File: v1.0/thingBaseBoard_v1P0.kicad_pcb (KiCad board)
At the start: 2 copper layers, 222 x 75 mm, 66 parts, among them P1 3_Pin_Screw_Connector, P2 16_PIN_IDC_HEADER, P3 8_Pin Screw Connector, Q1 2N3904-MMBT, Q2 2N3904-MMBT, Q3 2N3904-MMBT, Q4 2N3904-MMBT, Q5 2N3904-MMBT, Q6 2N3904-MMBT, Q7 2N7002, U1 HenLv-AC220S3_3DCS-3W, U2 DF08S1_BRIDGE_REC-IC, U3 XBEE_MODULE, U4 TRIAC_BOARD, U5 4N35_OPTO, U6 TRIAC_BOARD

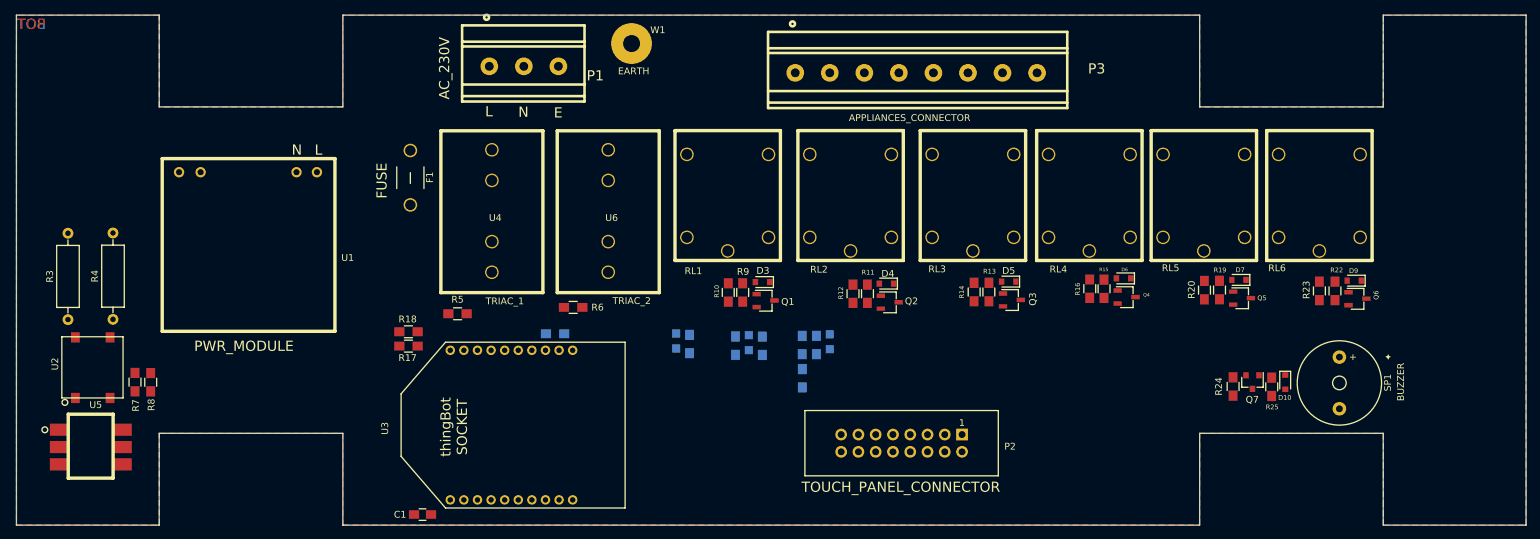
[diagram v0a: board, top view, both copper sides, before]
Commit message: Routing done
routing Completed,
Power Module footprint Changed,
2mm size of the PCB reduced.
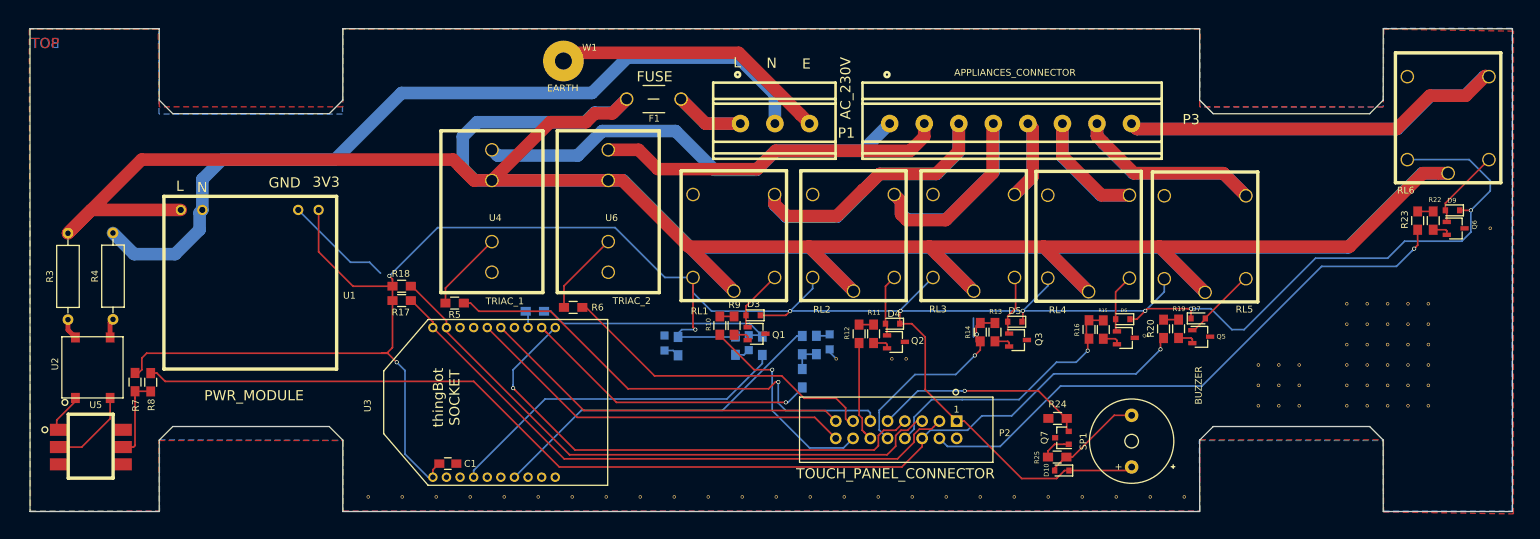
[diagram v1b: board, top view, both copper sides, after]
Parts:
- added REF**: VIA_0.5mm, via:VIA_0.5mm, F.Cu at (198.7, 126.3)
- added REF**: VIA_0.5mm, via:VIA_0.5mm, F.Cu at (153.7, 126.3)
- added REF**: VIA_0.5mm, via:VIA_0.5mm, F.Cu at (148.7, 126.3)
- added REF**: VIA_0.5mm, via:VIA_0.5mm, F.Cu at (143.7, 126.3)
- added REF**: VIA_0.5mm, via:VIA_0.5mm, F.Cu at (138.7, 126.3)
- added REF**: VIA_0.5mm, via:VIA_0.5mm, F.Cu at (133.7, 126.3)
- added REF**: VIA_0.5mm, via:VIA_0.5mm, F.Cu at (128.7, 126.3)
- added REF**: VIA_0.5mm, via:VIA_0.5mm, F.Cu at (123.7, 126.3)
- added REF**: VIA_0.5mm, via:VIA_0.5mm, F.Cu at (118.7, 126.3)
- added REF**: VIA_0.5mm, via:VIA_0.5mm, F.Cu at (113.7, 126.3)
- added REF**: VIA_0.5mm, via:VIA_0.5mm, F.Cu at (108.7, 126.3)
- added REF**: VIA_0.5mm, via:VIA_0.5mm, F.Cu at (193.7, 126.3)
- added REF**: VIA_0.5mm, via:VIA_0.5mm, F.Cu at (103.7, 126.3)
- added REF**: VIA_0.5mm, via:VIA_0.5mm, F.Cu at (98.7, 126.3)
- added REF**: VIA_0.5mm, via:VIA_0.5mm, F.Cu at (93.7, 126.3)
- added REF**: VIA_0.5mm, via:VIA_0.5mm, F.Cu at (88.7, 126.3)
- added REF**: VIA_0.5mm, via:VIA_0.5mm, F.Cu at (83.7, 126.3)
- added REF**: VIA_0.5mm, via:VIA_0.5mm, F.Cu at (78.7, 126.3)
- added REF**: VIA_0.5mm, via:VIA_0.5mm, F.Cu at (215.6, 106.9)
- added REF**: VIA_0.5mm, via:VIA_0.5mm, F.Cu at (209.6, 106.9)
- added REF**: VIA_0.5mm, via:VIA_0.5mm, F.Cu at (212.6, 106.9)
- added REF**: VIA_0.5mm, via:VIA_0.5mm, F.Cu at (215.6, 112.9)
- added REF**: VIA_0.5mm, via:VIA_0.5mm, F.Cu at (188.7, 126.3)
- added REF**: VIA_0.5mm, via:VIA_0.5mm, F.Cu at (212.6, 112.9)
- added REF**: VIA_0.5mm, via:VIA_0.5mm, F.Cu at (209.6, 112.9)
- added REF**: VIA_0.5mm, via:VIA_0.5mm, F.Cu at (215.6, 109.9)
- added REF**: VIA_0.5mm, via:VIA_0.5mm, F.Cu at (212.6, 109.9)
- added REF**: VIA_0.5mm, via:VIA_0.5mm, F.Cu at (209.6, 109.9)
- added REF**: VIA_0.5mm, via:VIA_0.5mm, F.Cu at (234.6, 112.9)
- added REF**: VIA_0.5mm, via:VIA_0.5mm, F.Cu at (231.6, 112.9)
- added REF**: VIA_0.5mm, via:VIA_0.5mm, F.Cu at (228.6, 112.9)
- added REF**: VIA_0.5mm, via:VIA_0.5mm, F.Cu at (225.6, 112.9)
- added REF**: VIA_0.5mm, via:VIA_0.5mm, F.Cu at (222.6, 112.9)
- added REF**: VIA_0.5mm, via:VIA_0.5mm, F.Cu at (183.7, 126.3)
- added REF**: VIA_0.5mm, via:VIA_0.5mm, F.Cu at (234.6, 109.9)
- added REF**: VIA_0.5mm, via:VIA_0.5mm, F.Cu at (231.6, 109.9)
- added REF**: VIA_0.5mm, via:VIA_0.5mm, F.Cu at (228.6, 109.9)
- added REF**: VIA_0.5mm, via:VIA_0.5mm, F.Cu at (225.6, 109.9)
- added REF**: VIA_0.5mm, via:VIA_0.5mm, F.Cu at (222.6, 109.9)
- added REF**: VIA_0.5mm, via:VIA_0.5mm, F.Cu at (234.6, 106.9)
- added REF**: VIA_0.5mm, via:VIA_0.5mm, F.Cu at (231.6, 106.9)
- added REF**: VIA_0.5mm, via:VIA_0.5mm, F.Cu at (228.6, 106.9)
- added REF**: VIA_0.5mm, via:VIA_0.5mm, F.Cu at (225.6, 106.9)
- added REF**: VIA_0.5mm, via:VIA_0.5mm, F.Cu at (222.6, 106.9)
- added REF**: VIA_0.5mm, via:VIA_0.5mm, F.Cu at (178.7, 126.3)
- added REF**: VIA_0.5mm, via:VIA_0.5mm, F.Cu at (234.6, 103.9)
- added REF**: VIA_0.5mm, via:VIA_0.5mm, F.Cu at (231.6, 103.9)
- added REF**: VIA_0.5mm, via:VIA_0.5mm, F.Cu at (228.6, 103.9)
- added REF**: VIA_0.5mm, via:VIA_0.5mm, F.Cu at (225.6, 103.9)
- added REF**: VIA_0.5mm, via:VIA_0.5mm, F.Cu at (222.6, 103.9)
- added REF**: VIA_0.5mm, via:VIA_0.5mm, F.Cu at (234.6, 100.9)
- added REF**: VIA_0.5mm, via:VIA_0.5mm, F.Cu at (231.6, 100.9)
- added REF**: VIA_0.5mm, via:VIA_0.5mm, F.Cu at (228.6, 100.9)
- added REF**: VIA_0.5mm, via:VIA_0.5mm, F.Cu at (225.6, 100.9)
- added REF**: VIA_0.5mm, via:VIA_0.5mm, F.Cu at (222.6, 100.9)
- added REF**: VIA_0.5mm, via:VIA_0.5mm, F.Cu at (173.7, 126.3)
- added REF**: VIA_0.5mm, via:VIA_0.5mm, F.Cu at (234.6, 97.9)
- added REF**: VIA_0.5mm, via:VIA_0.5mm, F.Cu at (231.6, 97.9)
- added REF**: VIA_0.5mm, via:VIA_0.5mm, F.Cu at (228.6, 97.9)
- added REF**: VIA_0.5mm, via:VIA_0.5mm, F.Cu at (225.6, 97.9)
- added REF**: VIA_0.5mm, via:VIA_0.5mm, F.Cu at (222.6, 97.9)
- added REF**: VIA_0.5mm, via:VIA_0.5mm, F.Cu at (155.7, 106.0)
- added REF**: VIA_0.5mm, via:VIA_0.5mm, F.Cu at (157.8, 106.0)
- added REF**: VIA_0.5mm, via:VIA_0.5mm, F.Cu at (147.5, 106.0)
- added REF**: VIA_0.5mm, via:VIA_0.5mm, F.Cu at (243.7, 86.8)
- added REF**: Fab Details table, Fab Details table:Fab Details table, F.Cu at (38.0, 145.6)
- added REF**: VIA_0.5mm, via:VIA_0.5mm, F.Cu at (168.7, 126.3)
- added REF**: VIA_0.5mm, via:VIA_0.5mm, F.Cu at (163.7, 126.3)
- added REF**: VIA_0.5mm, via:VIA_0.5mm, F.Cu at (158.7, 126.3)
- P1: value 3_Pin_Screw_Connector -> AC_230V
- P2: value 16_PIN_IDC_HEADER -> TOUCH_PANEL_CONNECTOR
- P3: value 8_Pin Screw Connector -> APPLIANCES_CONNECTOR
- moved F1 40.5 mm to (124.7, 67.8), turned to 180 degrees
- moved P1 37.9 mm to (133.4, 71.4)
- moved D10 35.3 mm to (180.7, 122.4), turned to 180 degrees
- moved R25 33.2 mm to (180.0, 120.4), turned to 0 degrees
- moved SP1 31.7 mm to (191.0, 118.1), turned to 90 degrees
- moved Q7 29.2 mm to (180.7, 117.6), turned to 180 degrees
- moved R24 26.2 mm to (180.1, 114.8), turned to 0 degrees
- moved RL6 22.1 mm to (245.6, 80.6)
- moved D9 17.8 mm to (238.2, 84.2)
- moved Q6 17.8 mm to (238.6, 86.8)
- moved R23 17.8 mm to (233.0, 85.7)
- moved R22 17.8 mm to (235.3, 85.7)
- moved P3 15.8 mm to (155.4, 71.4)
- moved W1 10.3 mm to (107.4, 62.2)
- moved C1 8.37 mm to (90.4, 121.4), turned to 0 degrees
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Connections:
- U1 pad 1: Net-(F1-Pad1) -> L
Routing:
- net L: track 0.00 -> 540.5 mm
- net +3V3: track 0.00 -> 403.3 mm, vias 0 -> 9
- net RELAY_5: track 0.00 -> 163.9 mm, vias 0 -> 1
- net N: track 0.00 -> 121.3 mm
- net Net-(P3-Pad8): track 0.00 -> 112.2 mm
- net I2C_SDA: track 0.00 -> 90.8 mm
- net I2C_SCL: track 0.00 -> 89.5 mm
- net RELAY_6: track 0.00 -> 85.3 mm, vias 0 -> 1
- net TOUCH_INTR: track 0.00 -> 75.5 mm, vias 0 -> 1
- net Net-(P3-Pad3): track 0.00 -> 74.7 mm
- net TRIAC_1: track 0.00 -> 70.3 mm, vias 0 -> 1
- net Net-(P3-Pad1): track 0.00 -> 65.5 mm
- net TS_INTR: track 0.00 -> 58.0 mm
- net LS_INTR: track 0.00 -> 54.9 mm
- net Net-(P3-Pad7): track 0.00 -> 54.8 mm
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- added copper zone on B.Cu, net GND
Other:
- board size 222 x 75 mm -> 218 x 71 mm
- net class AC_SUPPLY_3A added: clearance 0.5, trace_width 0.707, via_dia 1.5, via_drill 1.3
- net class AC_SUPPLY_6A added: clearance 0.5, trace_width 1.85, via_dia 3.4, via_drill 3.2
- net class SIGNALS added: clearance 0.2, trace_width 0.25, via_dia 0.6, via_drill 0.4
- board text added: "222 X 75"
- board text added: "3V3"
- board text added: "GND"

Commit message: Bom Create, Holes made in Layout, Schematic Changed
- Bom generated
- in schematic Mosfet Q7 Changed
- in layout mounting holes made
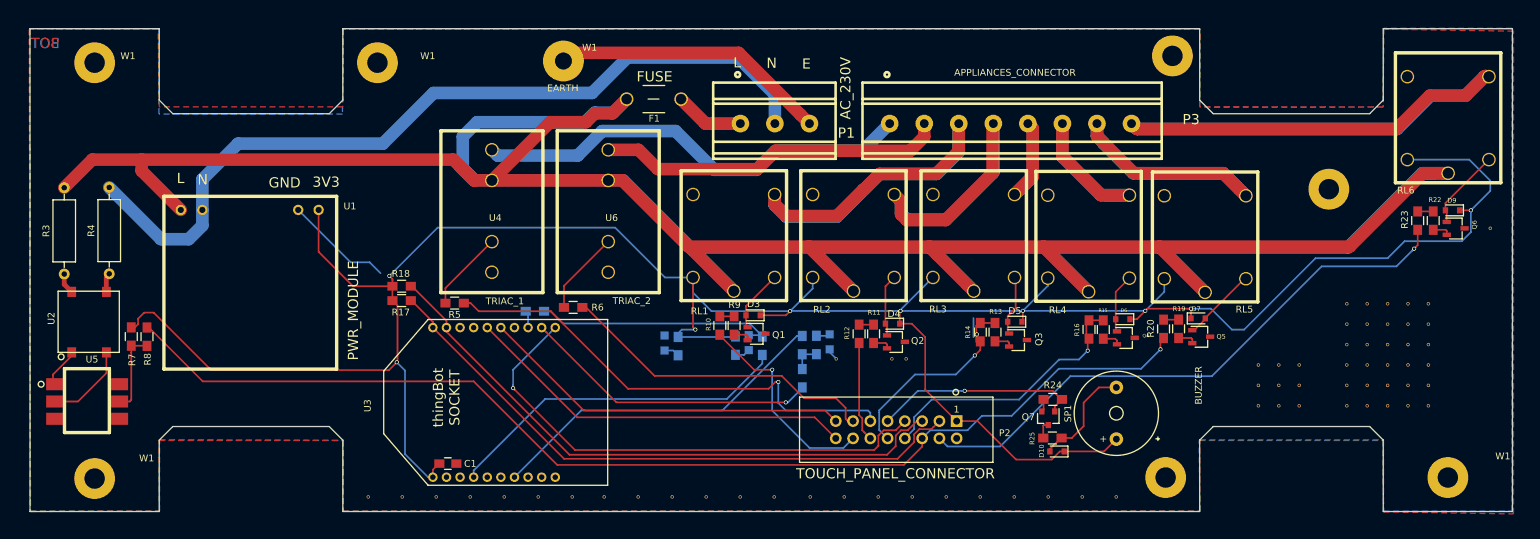
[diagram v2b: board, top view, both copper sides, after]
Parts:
- removed the REF** at (198.7, 126.3)
- removed the REF** at (193.7, 126.3)
- added W1: EARTH, Wire_Pads:SolderWirePad_single_2-5mmDrill, F.Cu at (224.6, 80.8)
- added W1: EARTH, Wire_Pads:SolderWirePad_single_2-5mmDrill, F.Cu at (42.2, 122.6)
- added W1: EARTH, Wire_Pads:SolderWirePad_single_2-5mmDrill, F.Cu at (241.7, 122.3)
- added W1: EARTH, Wire_Pads:SolderWirePad_single_2-5mmDrill, F.Cu at (201.6, 61.2)
- added W1: EARTH, Wire_Pads:SolderWirePad_single_2-5mmDrill, F.Cu at (200.8, 123.7)
- added W1: EARTH, Wire_Pads:SolderWirePad_single_2-5mmDrill, F.Cu at (83.6, 63.5)
- added W1: EARTH, Wire_Pads:SolderWirePad_single_2-5mmDrill, F.Cu at (39.5, 63.5)
- moved REF** 103.7 mm to (141.4, 153.2)
- moved R3 6.72 mm to (34.0, 93.5)
- moved R4 6.72 mm to (40.6, 93.5)
- moved R7 6.72 mm to (43.9, 102.7)
- moved R8 6.72 mm to (46.2, 102.7)
- moved U2 6.72 mm to (35.1, 105.0)
- moved U5 6.72 mm to (34.0, 107.4)
- moved SP1 4.68 mm to (188.7, 114.0)
- moved Q7 3.51 mm to (178.7, 114.7), turned to 270 degrees
- moved G*** 3.11 mm to (127.1, 117.0)
- moved R24 2.89 mm to (179.4, 112.0)
- moved D10 2.89 mm to (180.0, 119.6)
- moved R25 2.89 mm to (179.3, 117.6)
- moved REF** 0.30 mm to (123.4, 126.3)
- moved REF** 0.30 mm to (118.4, 126.3)
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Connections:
- Q7 pad 1: Net-(Q7-Pad1) -> BUZZER
- Q7 pad 2: BUZZER -> GND
- Q7 pad 3: GND -> Net-(Q7-Pad3)
- R25 pad 1: Net-(Q7-Pad1) -> Net-(Q7-Pad3)
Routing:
- net L: track 540.5 -> 530.0 mm
- net Net-(Q7-Pad1): track 4.36 -> 0.00 mm
- net RELAY_5: track 163.9 -> 167.0 mm
- net Net-(Q7-Pad3): track 0.00 -> 2.60 mm
- net GND: track 17.7 -> 19.6 mm
- net +3V3: track 403.3 -> 405.0 mm
- net BUZZER: track 31.9 -> 30.2 mm
- net N: track 121.3 -> 122.7 mm
- net Net-(D10-Pad2): track 14.9 -> 15.9 mm
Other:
- board text added: "218X 71"
- board text added: "Hole Dimensions : Outer Diameter = 6 mm Inner Diameter = 3 mm"
- board text removed: "222 X 75"
